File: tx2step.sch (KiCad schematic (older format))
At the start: 55 parts, among them IC1 ATMEGA328P-MM

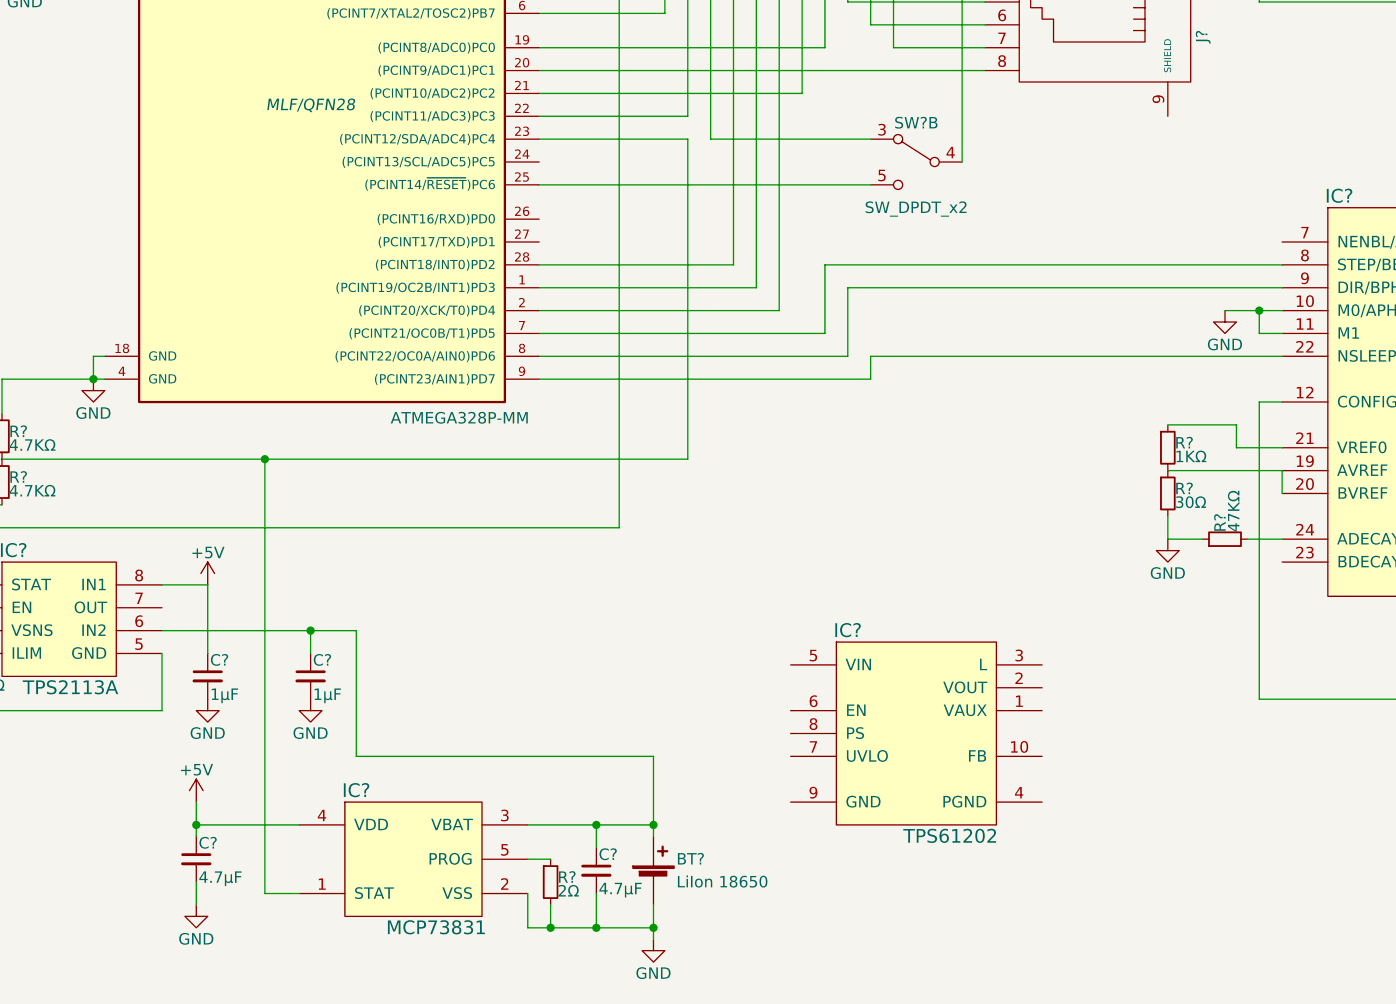
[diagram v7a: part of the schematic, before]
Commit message: Wire up TPS61202 boost regulator and power side of DPDT switch
The power supply circuit should now be complete.
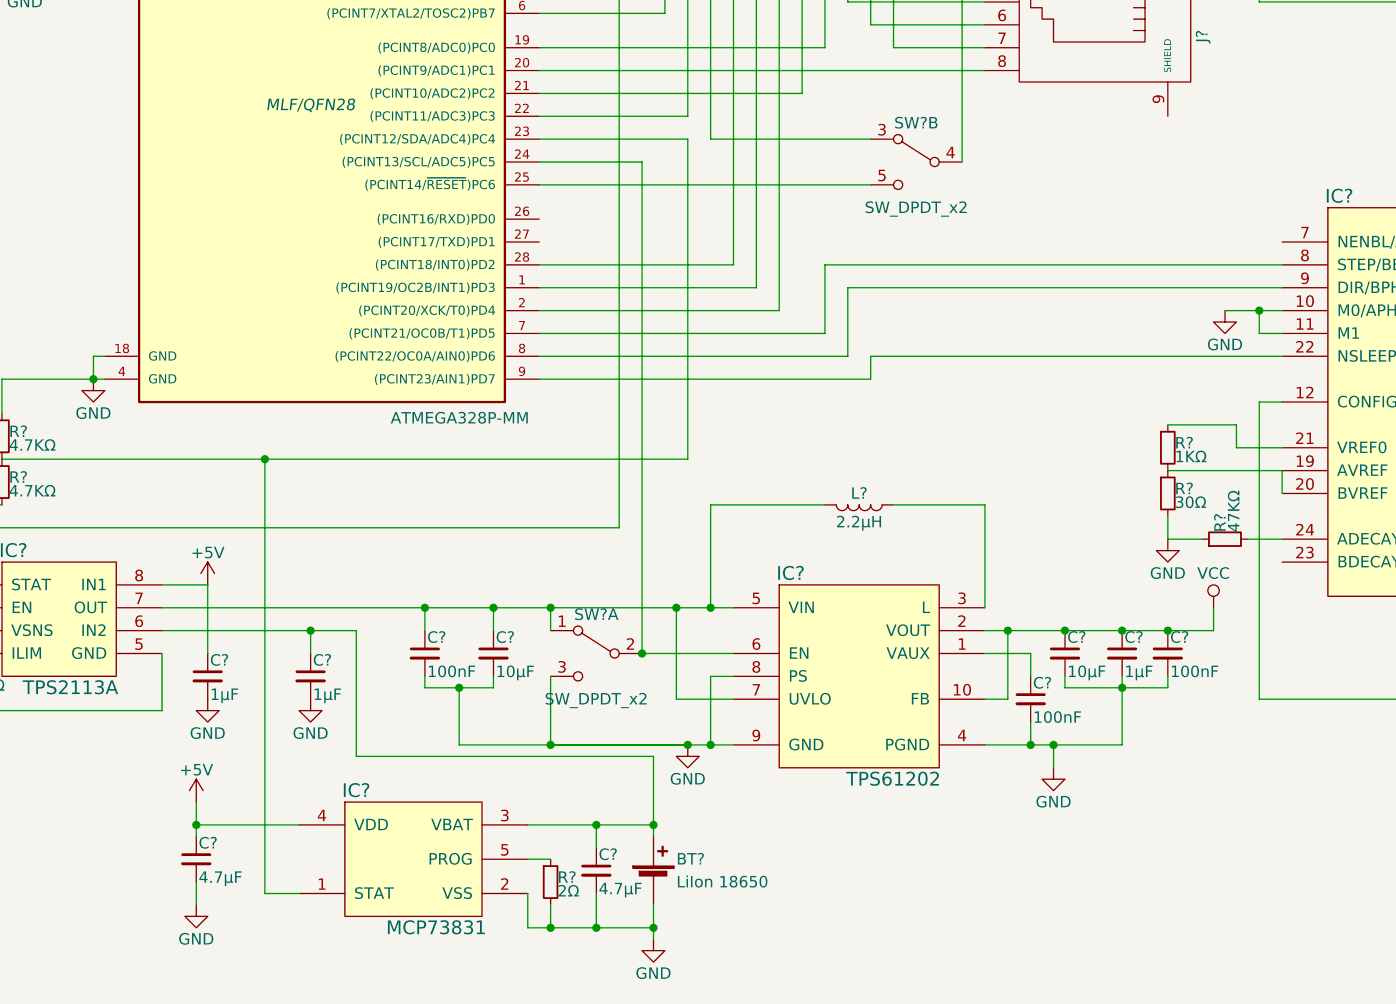
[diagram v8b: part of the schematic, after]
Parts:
- added C? (x3): 100nF, symbol C_Small
- added C? (x2): 10µF, symbol C_Small
- added C?: 1µF, symbol C_Small
- added L?: 2.2µH, symbol L
- added SW?: SW_DPDT_x2, symbol SW_DPDT_x2
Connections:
- net GND: now also IC?.4 (PGND), IC?.8 (PS), IC?.9 (GND), C?.2, C?.2, C?.2, C?.2, C?.2, C?.2, SW?.3 (C)
- net VCC: now also IC?.10 (FB), IC?.2 (VOUT), C?.1, C?.1, C?.1
- net at IC1.24 ((PCINT13/SCL/ADC5)PC5): now also IC?.6 (EN), SW?.2 (B)
- net at IC?.1 (VAUX): now also C?.1
- net at IC?.3 (L): now also L?.1
- net at IC?.5 (VIN): now also IC?.7 (OUT), IC?.7 (UVLO), C?.1, C?.1, L?.2, SW?.1 (A)
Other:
- moved on the sheet: IC?
